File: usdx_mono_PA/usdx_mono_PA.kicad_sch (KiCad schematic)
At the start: 58 parts, among them J1 Conn_01x04, J2 Conn_01x01, J3 Conn_01x04, J4 Conn_01x02, J5 Conn_01x02, K1 IM01, K2 IM01, Q1 IRF530, Q2 DTC114EE, Q3 DTC114EE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

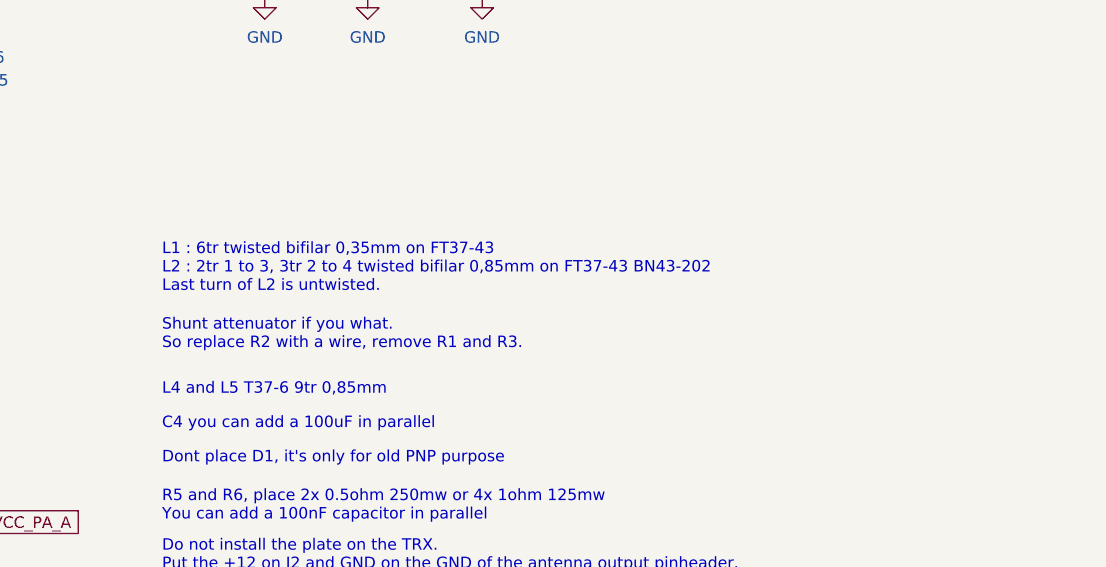
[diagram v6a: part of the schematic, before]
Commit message: add measures and eliptic low pass filter modifications
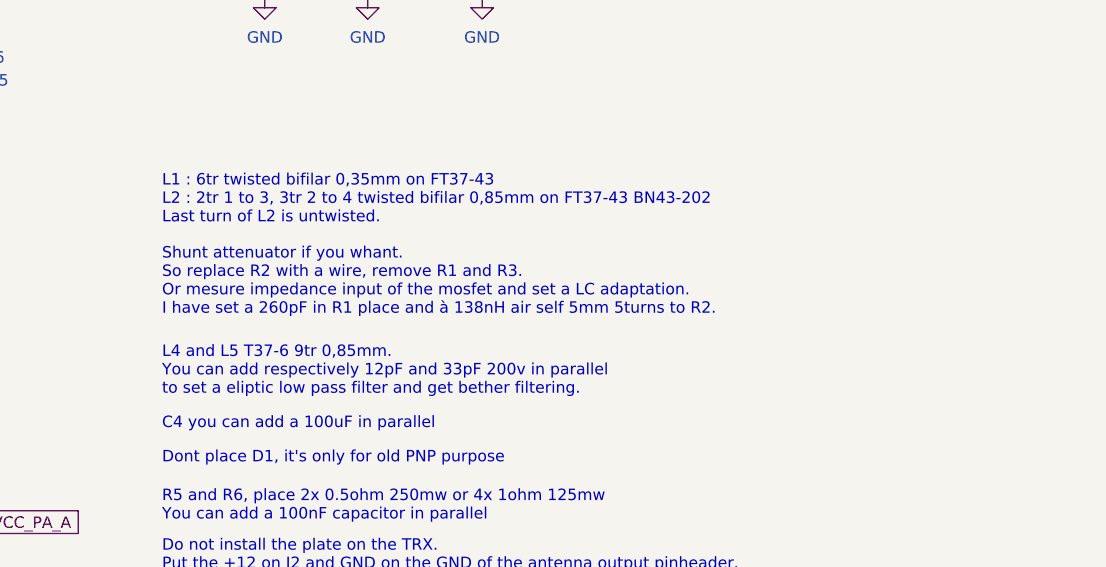
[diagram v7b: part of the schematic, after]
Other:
- note added: "L4 and L5 T37-6 9tr 0,85mm. You can add respectively 12pF and 33pF 200v in parallel to set a eliptic low pass filter and get bether filtering."
- note added: "Shunt attenuator if you whant. So replace R2 with a wire, remove R1 and R3. Or mesure impedance input of the mosfet and set a LC adaptation. I have set a 260pF in R1 place and à 138nH air self 5mm 5turns to R2."
- note removed: "L4 and L5 T37-6 9tr 0,85mm"
- note removed: "Shunt attenuator if you what. So replace R2 with a wire, remove R1 and R3."
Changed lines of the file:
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@@
     (stroke (width 0) (type default) (color 0 0 0 0))
   )
-  (text "L4 and L5 T37-6 9tr 0,85mm" (at 179.07 115.57 0)
+  (text "L4 and L5 T37-6 9tr 0,85mm. \nYou can add respectively 12pF and 33pF 200v in parallel \nto set a eliptic low pass filter and get bether filtering."
+    (at 179.07 115.57 0)
     (effects (font (size 1.27 1.27)) (justify left bottom))
   )
@@
     (effects (font (size 1.27 1.27)) (justify left bottom))
   )
-  (text "Shunt attenuator if you what.\nSo replace R2 with a wire, remove R1 and R3."
-    (at 179.07 110.49 0)
+  (text "Shunt attenuator if you whant.\nSo replace R2 with a wire, remove R1 and R3. \nOr mesure impedance input of the mosfet and set a LC adaptation.\nI have set a 260pF in R1 place and à 138nH air self 5mm 5turns to R2."
+    (at 179.07 106.68 0)
     (effects (font (size 1.27 1.27)) (justify left bottom))
   )
@@
   )
   (text "L1 : 6tr twisted bifilar 0,35mm on FT37-43\nL2 : 2tr 1 to 3, 3tr 2 to 4 twisted bifilar 0,85mm on FT37-43 BN43-202\nLast turn of L2 is untwisted."
-    (at 179.07 104.14 0)
+    (at 179.07 96.52 0)
     (effects (font (size 1.27 1.27)) (justify left bottom))
   )
